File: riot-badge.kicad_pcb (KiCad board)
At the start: 4 copper layers, 99.1 x 99.1 mm, 406 parts, among them J1 SAO, J2 UEXT, J3 SWD, J4 3.5 mm "CAN" Connector, J5 USB_C_Receptacle_USB2.0_16P, J6 BAT, SW1 SW_Push, SW10 SW_Push, SW2 SW_Push, SW3 SW_Push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

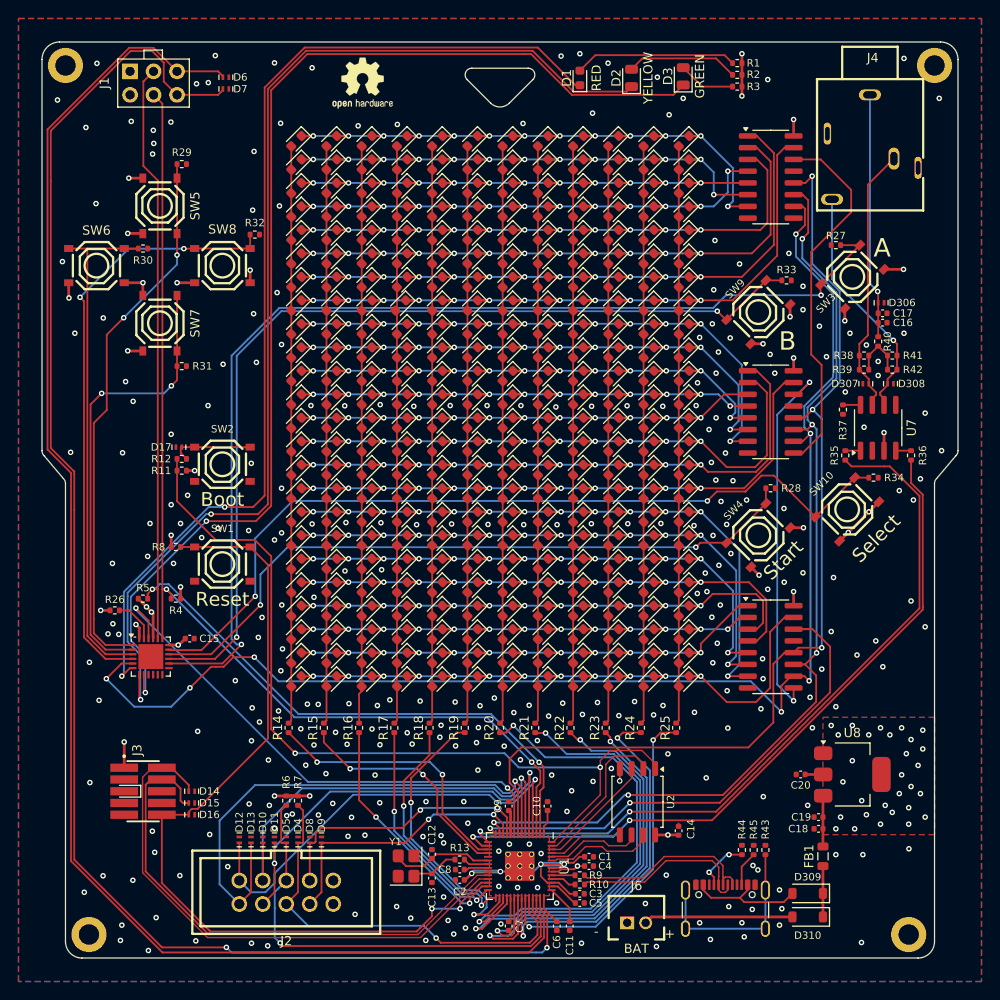
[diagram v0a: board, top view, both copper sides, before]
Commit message: board: updated to schematics
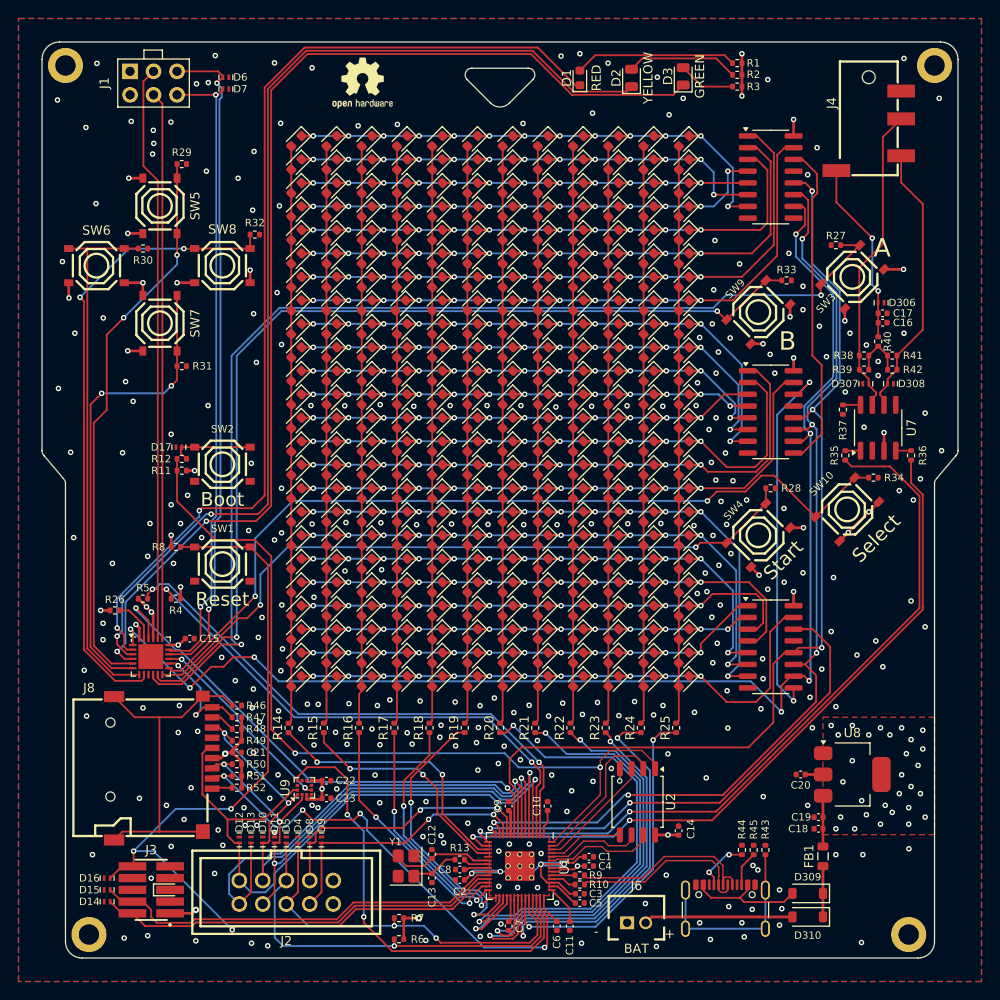
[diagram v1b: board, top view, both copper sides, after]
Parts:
- added C21: 100 nF, Capacitor_SMD:C_0402_1005Metric, F.Cu at (46.5, 102.2)
- added C22: 100 nF, Capacitor_SMD:C_0402_1005Metric, F.Cu at (56.2, 105.3)
- added C23: 100 nF, Capacitor_SMD:C_0402_1005Metric, F.Cu at (56.2, 107.2)
- added J8: uSD card, custom:uSD_CARD, F.Cu at (38.5, 103.9)
- added R46: 1M, Resistor_SMD:R_0402_1005Metric, F.Cu at (46.5, 97.2)
- added R47: 10 K, Resistor_SMD:R_0402_1005Metric, F.Cu at (46.5, 98.4)
- added R48: 47K, Resistor_SMD:R_0402_1005Metric, F.Cu at (46.5, 99.7)
- added R49: 47K, Resistor_SMD:R_0402_1005Metric, F.Cu at (46.5, 101.0)
- added R50: 47K, Resistor_SMD:R_0402_1005Metric, F.Cu at (46.5, 103.5)
- added R51: 47K, Resistor_SMD:R_0402_1005Metric, F.Cu at (46.5, 104.8)
- added R52: 47K, Resistor_SMD:R_0402_1005Metric, F.Cu at (46.5, 106.0)
- added U9: SC7A20, Package_LGA:LGA-12_2x2mm_P0.5mm, F.Cu at (53.8, 106.0)
- J4: footprint custom:AUDIO-TH_PJ324 -> custom:Jack_3.5mm_PJ-320D
- moved R6 19.3 mm to (64.0, 122.4), turned to 180 degrees
- moved R7 16.8 mm to (64.0, 120.1), turned to 180 degrees
- moved D14 15.0 mm to (32.4, 118.4), turned to 180 degrees
- moved D15 13.1 mm to (32.4, 117.1), turned to 180 degrees
- moved D16 11.4 mm to (32.4, 115.8), turned to 180 degrees
- moved J3 10.7 mm to (37.2, 117.1), turned to 90 degrees
- moved J4 1.81 mm to (114.8, 35.0)
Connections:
- net /SPI0_CS renamed /SPI0_UEXT_~{CS}
- U1 pad 40: /SAO_GPIO1 -> /SPI0_ACCEL_~{CS}
- U1 pad 41: /SAO_GPIO2 -> /SPI0_SD_~{CS}
- U6 pad 1: /GPIO Extender/BTN_UP -> /DISP_~{SRCLR}
- U6 pad 10: /GPIO Extender/GPIO0_4 -> /GPIO Extender/BTN_A
- U6 pad 11: /GPIO Extender/GPIO0_5 -> /GPIO Extender/BTN_B
- U6 pad 12: /GPIO Extender/GPIO0_6 -> /GPIO Extender/BTN_START
- U6 pad 13: /GPIO Extender/GPIO0_7 -> /GPIO Extender/BTN_SELECT
- U6 pad 14: /GPIO Extender/BTN_A -> /SD_~{CARD_DET}
- U6 pad 15: /GPIO Extender/BTN_B -> /ACCEL_INT
- U6 pad 16: /GPIO Extender/BTN_START -> /SAO_GPIO1
- U6 pad 17: /GPIO Extender/BTN_SELECT -> /SAO_GPIO2
- U6 pad 2: /GPIO Extender/BTN_DOWN -> /LED_RED
- U6 pad 3: /GPIO Extender/BTN_LEFT -> /LED_YELLOW
- U6 pad 4: /GPIO Extender/BTN_RIGHT -> /LED_GREEN
- U6 pad 5: /DISP_~{SRCLR} -> /GPIO Extender/BTN_UP
- U6 pad 6: /LED_RED -> /GPIO Extender/BTN_DOWN
- U6 pad 7: /LED_YELLOW -> /GPIO Extender/BTN_LEFT
- U6 pad 8: /LED_GREEN -> /GPIO Extender/BTN_RIGHT
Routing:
- net /SAO_GPIO2: track 166.8 -> 69.0 mm
- net /SAO_GPIO1: track 164.7 -> 72.0 mm, vias 0 -> 2
- net /SPI0_SD_~{CS}: track 0.00 -> 53.2 mm, vias 0 -> 4
- net /SPI0_ACCEL_~{CS}: track 0.00 -> 49.0 mm, vias 0 -> 2
- net Net-(J8-SHIELD): track 0.00 -> 37.4 mm
- net /SPI0_SCK: track 49.1 -> 70.9 mm
- net /ACCEL_INT: track 0.00 -> 21.6 mm, vias 0 -> 2
- net /SPI0_CIPO: track 47.4 -> 65.2 mm, vias 1 -> 3
- net /SPI0_COPI: track 47.8 -> 64.6 mm, vias 2 -> 4
- net /SWDIO: track 60.1 -> 44.1 mm
- net +3.3V: track 90.7 -> 105.9 mm, vias 70 -> 71
- net /SWDCLK: track 58.6 -> 44.9 mm
- net /SD_~{CARD_DET}: track 0.00 -> 12.4 mm, vias 0 -> 2
- net /~{RESET}: track 91.9 -> 99.3 mm, vias 2 -> 3
- net /LED_YELLOW: track 122.0 -> 115.3 mm
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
